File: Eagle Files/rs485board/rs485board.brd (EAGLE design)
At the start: 63.5 x 63.5 mm, 81 parts, among them IC1 XC6206P332MR, IC2 MP2359, J1 AVR_SPI_PROG_3X2PTH, J2 RA 6Pin SMD, Q1 CJ3404, Q2 CJ3404, Q3 CJ3404, U1 ATMEGA328P_TQFP, U2 LIS3DH, U3 MAX3485CSA, X1 RJ45-8P8C-8L-B, X3 RJ45-8P8C-8L-B, Y1 16MHz

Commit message: add values
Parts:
- C1, C11, C14, C15, C16, C17, C18, C19, C20, C21, C22, C23, C24, C25, C26, C3, C4, C5, C7, C8, C9: value (none) -> 0.1uF
- C10: value (none) -> 10nF
- C12, C2, C6: value (none) -> 10uF
- R1, R10, R5, R6, R7: value (none) -> 10K
- R11: value (none) -> 120
- R12, R13: value (none) -> 1K
- R2, R3, R4: value (none) -> DNP
- R8, R9: value (none) -> 51K

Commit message: add value and gerber
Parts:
- D1, D19, D2, D3, D4, D5, D6: value (none) -> 5819
- U3: value MAX3485CSA -> SP485
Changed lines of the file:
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@@
 <attribute name="VALUE" x="41.91" y="7.366" size="0.6096" layer="27" font="vector" ratio="20" align="top-left"/>
 </element>
-<element name="D1" library="adafruit" library_urn="urn:adsk.eagle:library:420" package="SOD-123" value="" x="8.128" y="23.876" smashed="yes" rot="R90">
+<element name="D1" library="adafruit" library_urn="urn:adsk.eagle:library:420" package="SOD-123" value="5819" x="8.128" y="23.876" smashed="yes" rot="R90">
 <attribute name="NAME" x="7.282" y="19.542" size="0.8128" layer="25"/>
 <attribute name="VALUE" x="9.412" y="22.776" size="0.4064" layer="27" rot="R90"/>
@@
 <attribute name="VALUE" x="10.668" y="28.575" size="1.27" layer="27" rot="R90"/>
 </element>
-<element name="D2" library="adafruit" library_urn="urn:adsk.eagle:library:420" package="SOD-123" value="" x="4.064" y="23.876" smashed="yes" rot="R90">
+<element name="D2" library="adafruit" library_urn="urn:adsk.eagle:library:420" package="SOD-123" value="5819" x="4.064" y="23.876" smashed="yes" rot="R90">
 <attribute name="NAME" x="3.218" y="19.542" size="0.8128" layer="25"/>
 <attribute name="VALUE" x="5.348" y="22.776" size="0.4064" layer="27" rot="R90"/>
 </element>
-<element name="D3" library="adafruit" library_urn="urn:adsk.eagle:library:420" package="SOD-123" value="" x="6.096" y="23.876" smashed="yes" rot="R90">
+<element name="D3" library="adafruit" library_urn="urn:adsk.eagle:library:420" package="SOD-123" value="5819" x="6.096" y="23.876" smashed="yes" rot="R90">
 <attribute name="NAME" x="5.25" y="19.542" size="0.8128" layer="25"/>
 <attribute name="VALUE" x="7.38" y="22.776" size="0.4064" layer="27" rot="R90"/>
 </element>
-<element name="D4" library="adafruit" library_urn="urn:adsk.eagle:library:420" package="SOD-123" value="" x="2.032" y="23.876" smashed="yes" rot="R90">
+<element name="D4" library="adafruit" library_urn="urn:adsk.eagle:library:420" package="SOD-123" value="5819" x="2.032" y="23.876" smashed="yes" rot="R90">
 <attribute name="NAME" x="1.186" y="19.542" size="0.8128" layer="25"/>
 <attribute name="VALUE" x="3.316" y="22.776" size="0.4064" layer="27" rot="R90"/>
@@
 <attribute name="VALUE" x="4.572" y="28.575" size="1.27" layer="27" rot="R90"/>
 </element>
-<element name="D5" library="adafruit" library_urn="urn:adsk.eagle:library:420" package="SOD-123" value="" x="12.7" y="23.876" smashed="yes" rot="R90">
+<element name="D5" library="adafruit" library_urn="urn:adsk.eagle:library:420" package="SOD-123" value="5819" x="12.7" y="23.876" smashed="yes" rot="R90">
 <attribute name="NAME" x="12.108" y="20.304" size="0.8128" layer="25"/>
 <attribute name="VALUE" x="13.984" y="22.776" size="0.4064" layer="27" rot="R90"/>
 </element>
-<element name="D6" library="adafruit" library_urn="urn:adsk.eagle:library:420" package="SOD-123" value="" x="10.414" y="23.876" smashed="yes" rot="R90">
+<element name="D6" library="adafruit" library_urn="urn:adsk.eagle:library:420" package="SOD-123" value="5819" x="10.414" y="23.876" smashed="yes" rot="R90">
 <attribute name="NAME" x="9.568" y="20.304" size="0.8128" layer="25"/>
 <attribute name="VALUE" x="11.698" y="22.776" size="0.4064" layer="27" rot="R90"/>
 </element>
-<element name="U3" library="SparkFun-IC-Comms" package="SO08" value=" MAX3485CSA" x="57.15" y="31.75" smashed="yes">
+<element name="U3" library="SparkFun-IC-Comms" package="SO08" value="SP485" x="57.15" y="31.75" smashed="yes">
 <attribute name="NAME" x="53.975" y="31.75" size="0.8128" layer="25" font="vector" ratio="20" rot="R90" align="bottom-center"/>
 <attribute name="PROD_ID" value="IC-09388" x="57.15" y="31.75" size="1.778" layer="27" display="off"/>
@@
 <attribute name="PROD_ID" value="NDUC-13770" x="37.084" y="56.134" size="1.778" layer="27" rot="R90" display="off"/>
 </element>
-<element name="D19" library="adafruit" library_urn="urn:adsk.eagle:library:420" package="SOD-123" value="" x="32.258" y="52.832" smashed="yes" rot="R180">
+<element name="D19" library="adafruit" library_urn="urn:adsk.eagle:library:420" package="SOD-123" value="5819" x="32.258" y="52.832" smashed="yes" rot="R180">
 <attribute name="NAME" x="33.358" y="51.832" size="0.8128" layer="25" rot="R180"/>
 <attribute name="VALUE" x="33.358" y="54.116" size="0.4064" layer="27" rot="R180"/>

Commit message: add resistor
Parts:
- added R14: 10K, resistor:R0805
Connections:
- net +5V: now also R14.2
- net RX: now also R14.1
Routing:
- net RX: track 68.0 -> 74.7 mm
- net +5V: track 364.3 -> 366.5 mm
- net GND: track 623.1 -> 625.2 mm
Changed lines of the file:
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@@
 <?xml version="1.0" encoding="utf-8"?>
 <!DOCTYPE eagle SYSTEM "eagle.dtd">
-<eagle version="8.3.2">
+<eagle version="8.7.0">
 <drawing>
 <settings>
@@
 <param name="dpMaxLengthDifference" value="10mm"/>
 <param name="dpGapFactor" value="2.5"/>
-<param name="checkGrid" value="0"/>
 <param name="checkAngle" value="0"/>
 <param name="checkFont" value="1"/>
 <param name="checkRestrict" value="1"/>
+<param name="checkStop" value="0"/>
+<param name="checkValues" value="0"/>
 <param name="useDiameter" value="13"/>
 <param name="maxErrors" value="50"/>
@@
 <attribute name="OC_FARNELL" value="1279843" x="52.07" y="53.34" size="1.778" layer="28" rot="MR160" display="off"/>
 <attribute name="OC_NEWARK" value="52K4445" x="52.07" y="53.34" size="1.778" layer="28" rot="MR160" display="off"/>
+</element>
+<element name="R14" library="resistor" library_urn="urn:adsk.eagle:library:348" package="R0805" package3d_urn="urn:adsk.eagle:package:26059/1" value="10K" x="46.482" y="11.43" smashed="yes" rot="R270">
+<attribute name="NAME" x="45.339" y="13.462" size="0.8128" layer="25"/>
+<attribute name="VALUE" x="45.593" y="8.382" size="0.8128" layer="27"/>
 </element>
 </elements>
@@
 <contactref element="U3" pad="5"/>
 <contactref element="C26" pad="2"/>
-<wire x1="44.958" y1="10.414" x2="44.958" y2="7.62" width="0.254" layer="1"/>
+<wire x1="44.958" y1="10.414" x2="44.958" y2="10.16" width="0.254" layer="1"/>
+<wire x1="44.958" y1="10.16" x2="44.958" y2="7.62" width="0.254" layer="1"/>
 <wire x1="44.958" y1="7.62" x2="44.704" y2="7.366" width="0.254" layer="1"/>
 <wire x1="44.704" y1="7.366" x2="44.704" y2="2.794" width="0.254" layer="1"/>
 <wire x1="49.61" y1="15.24" x2="48.26" y2="15.24" width="0.254" layer="1"/>
-<wire x1="48.26" y1="15.24" x2="45.72" y2="12.7" width="0.254" layer="1"/>
-<wire x1="45.72" y1="12.7" x2="45.72" y2="11.176" width="0.254" layer="1"/>
-<wire x1="45.72" y1="11.176" x2="44.958" y2="10.414" width="0.254" layer="1"/>
 <contactref element="D17" pad="3"/>
 <contactref element="C24" pad="2"/>
@@
 <vertex x="0" y="0"/>
 </polygon>
+<wire x1="49.61" y1="15.24" x2="46.99" y2="15.24" width="0.254" layer="1"/>
+<wire x1="46.99" y1="15.24" x2="44.958" y2="13.208" width="0.254" layer="1"/>
+<wire x1="44.958" y1="13.208" x2="44.958" y2="10.414" width="0.254" layer="1"/>
 </signal>
 <signal name="RESET_EXT">
@@
 <wire x1="49.61" y1="7.62" x2="51.308" y2="7.62" width="0.254" layer="1"/>
 <wire x1="51.308" y1="7.62" x2="52.07" y2="8.382" width="0.254" layer="1"/>
-<wire x1="52.07" y1="17.018" x2="52.07" y2="8.382" width="0.254" layer="1"/>
+<wire x1="52.07" y1="17.018" x2="52.07" y2="13.97" width="0.254" layer="1"/>
+<wire x1="52.07" y1="13.97" x2="52.07" y2="8.382" width="0.254" layer="1"/>
 <wire x1="46.99" y1="18.034" x2="47.752" y2="18.034" width="0.254" layer="1"/>
 <wire x1="47.752" y1="18.034" x2="48.514" y2="18.796" width="0.254" layer="1"/>
@@
 <wire x1="51.882" y1="24.704" x2="54.61" y2="24.704" width="0.254" layer="1"/>
 <wire x1="48.514" y1="19.558" x2="50.8" y2="21.844" width="0.254" layer="1"/>
+<contactref element="R14" pad="1"/>
+<wire x1="46.482" y1="12.38" x2="46.482" y2="13.208" width="0.254" layer="1"/>
+<wire x1="46.482" y1="13.208" x2="47.244" y2="13.97" width="0.254" layer="1"/>
+<wire x1="47.244" y1="13.97" x2="52.07" y2="13.97" width="0.254" layer="1"/>
 </signal>
 <signal name="TX">
@@
 <wire x1="45.974" y1="6.096" x2="46.228" y2="6.35" width="0.508" layer="16"/>
 <wire x1="32.64803125" y1="6.096" x2="45.974" y2="6.096" width="0.508" layer="16"/>
-<wire x1="49.61" y1="10.16" x2="47.498" y2="10.16" width="0.254" layer="1"/>
-<wire x1="47.498" y1="10.16" x2="45.974" y2="8.636" width="0.254" layer="1"/>
-<wire x1="45.974" y1="8.636" x2="45.974" y2="6.604" width="0.254" layer="1"/>
-<wire x1="45.974" y1="6.604" x2="46.228" y2="6.35" width="0.254" layer="1"/>
+<wire x1="49.470946875" y1="10.12198125" x2="49.61" y2="10.16" width="0.254" layer="1"/>
 <contactref element="C20" pad="1"/>
 <contactref element="D13" pad="1"/>
@@
 <wire x1="22.606" y1="40.386" x2="5.08" y2="40.386" width="0.508" layer="16"/>
 <wire x1="5.08" y1="40.386" x2="2.032" y2="37.338" width="0.508" layer="16"/>
+<contactref element="R14" pad="2"/>
+<wire x1="46.228" y1="6.35" x2="46.228" y2="7.366" width="0.254" layer="1"/>
+<wire x1="48.98398125" y1="10.12198125" x2="49.470946875" y2="10.12198125" width="0.254" layer="1"/>
+<wire x1="46.228" y1="7.366" x2="48.98398125" y2="10.12198125" width="0.254" layer="1"/>
+<wire x1="49.61" y1="10.16" x2="46.802" y2="10.16" width="0.254" layer="1"/>
+<wire x1="46.802" y1="10.16" x2="46.482" y2="10.48" width="0.254" layer="1"/>
 </signal>
 <signal name="D9">

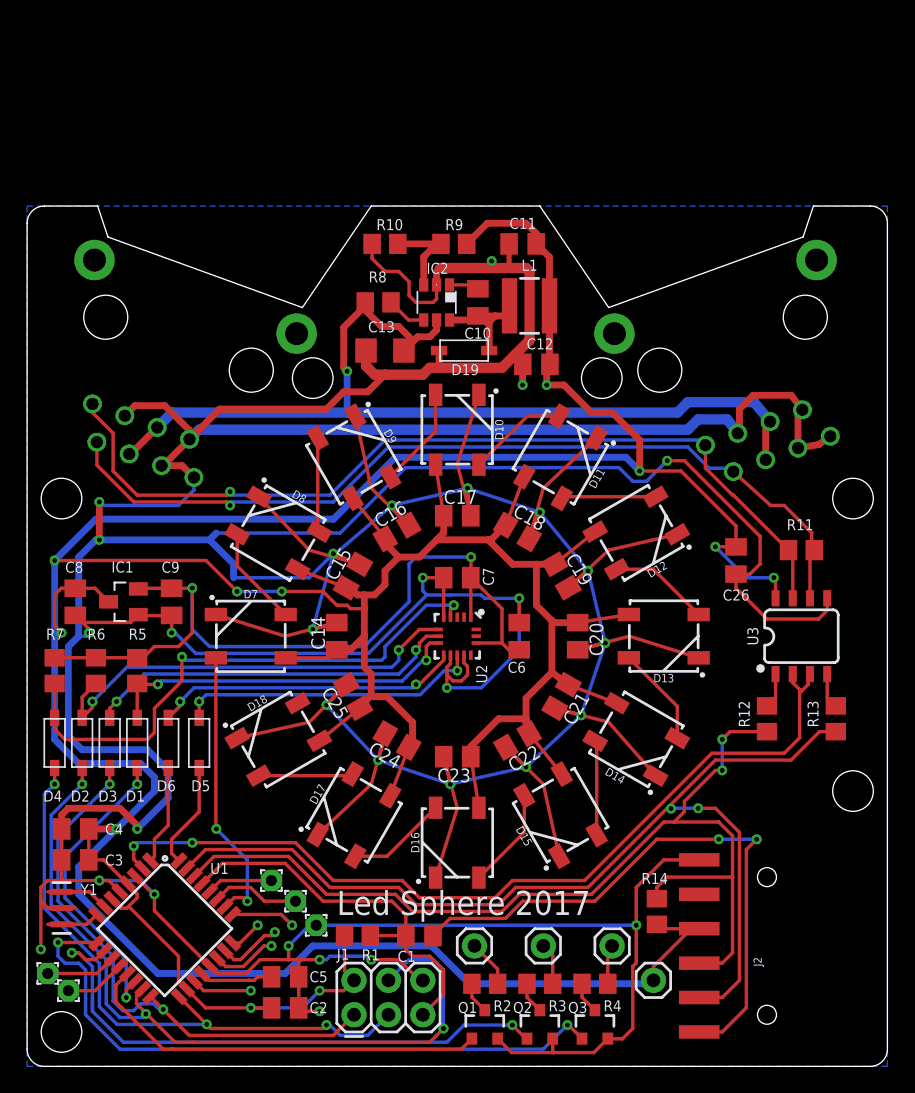
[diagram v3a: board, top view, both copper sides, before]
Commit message: 48V upgrade
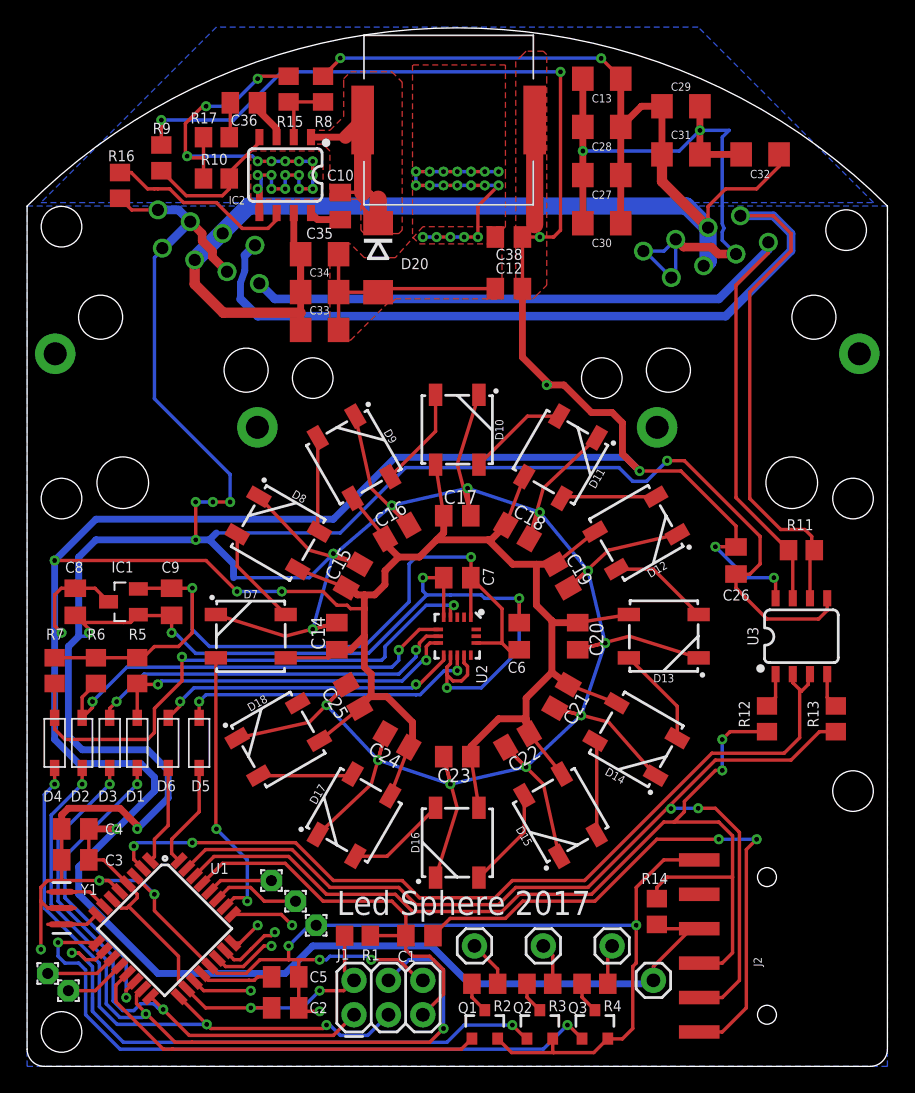
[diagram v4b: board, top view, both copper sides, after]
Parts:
- removed C11: 0.1uF, resistor:C0805K
- removed D19: 5819, adafruit:SOD-123
- added C27, C28, C29, C30, C31, C32, C33, C34, C35: 1uF 100V, SparkFun-Capacitors:1206
- added C36: 150pF, resistor:C0805K
- added C38: 10uF, resistor:C0805K
- added D20: B280-13-F, diode:DO214AA
- added R15: 17.4K, resistor:R0805
- added R16: 200K, resistor:R0805
- added R17: 158K, resistor:R0805
- C10: value 10nF -> 0.1uF
- C13: value 10uF -> 1uF 100V
- IC2: value MP2359 -> MP2562; device lmrdcdc-0.1:SOT23-6 -> misc:SO08
- L1: value 4.7uH -> 15uH; device SparkFun-Coils:INDUCTOR_4X4MM -> misc:SLF12575
- R10: value 10K -> 40.2k
- R8: value 51K -> 100K
- R9: value 51K -> 210K
- moved C13 25.7 mm to (42.4, 72.9)
- moved R9 22.5 mm to (9.91, 67.1), turned to 90 degrees
- moved R8 16.3 mm to (21.8, 72.1), turned to 90 degrees
- moved L1 15.0 mm to (31.1, 69.8), turned to 0 degrees
- moved IC2 14.6 mm to (19.1, 65.8)
- moved R10 13.3 mm to (14.0, 65.5)
- moved C10 12.4 mm to (23.1, 63.5), turned to 90 degrees
- moved C12 5.95 mm to (35.6, 57.4)
- moved X1 0.63 mm to (52.7, 53.3), turned to 340 degrees
- moved X3 0.38 mm to (10.8, 53.3), turned to 20 degrees
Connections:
- removed net N$18: C10.2, D19.C, IC2.6, L1.P$1
- removed net N$19: C10.1, IC2.1
- removed net N$21: IC2.3, R10.2, R9.1
- removed net N$23: IC2.4, R8.1
- new net BST: C10.1, IC2.8
- new net COMP: C36.1, IC2.3
- new net EN: IC2.2, R15.2, R8.1
- new net FB: IC2.4, R10.2, R9.1
- new net FREQ: IC2.6, R16.2
- new net N$25: C36.2, R17.2
- new net SW: C10.2, D20.C, IC2.1, L1.P$1
- net +24V: now also C27.1, C28.1, C29.1, C30.1, C31.1, C32.1, C33.1, C34.1, C35.1, IC2.7; no longer IC2.5
- net +5V: now also C38.1; no longer C11.1
- net GND: now also C27.2, C28.2, C29.2, C30.2, C31.2, C32.2, C33.2, C34.2, C35.2, C38.2, D20.A, IC2.5, R15.1, R16.1, R17.1; no longer C11.2, D19.A, IC2.2
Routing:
- net +24V: track 70.1 -> 122.2 mm, vias 1 -> 2
- net +5V: track 366.5 -> 417.0 mm, vias 11 -> 14
- net GND: track 625.2 -> 656.4 mm, vias 31 -> 70
- net RS485A: track 65.2 -> 88.7 mm, vias 1 -> 0
- net SW: track 0.00 -> 17.2 mm
- net FREQ: track 0.00 -> 14.0 mm
- net FB: track 0.00 -> 10.8 mm
- net N$18: track 10.8 -> 0.00 mm
- net N$21: track 6.60 -> 0.00 mm
- net EN: track 0.00 -> 5.30 mm
- net COMP: track 0.00 -> 3.12 mm
- net N$23: track 2.96 -> 0.00 mm
- net RS485B: track 66.2 -> 69.1 mm, vias 1 -> 0
- net N$25: track 0.00 -> 2.57 mm
- net BST: track 0.00 -> 2.36 mm
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- added copper zone on layer 1, net +5V
- added copper zone on layer 1, net GND
- added copper zone on layer 1, net SW
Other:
- board size 63.5 x 63.5 mm -> 63.5 x 76.7 mm
